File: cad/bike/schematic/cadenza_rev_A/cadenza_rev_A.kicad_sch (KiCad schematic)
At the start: 36 parts, among them J1 USB_A, J2 USB_C_Receptacle, J3 Conn_01x02, Q1 BC547, U1 TLC5916, U10 HDSP-A151, U11 TLC5916, U12 HDSP-A151, U13 STM32F105RCTx, U14 INA193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

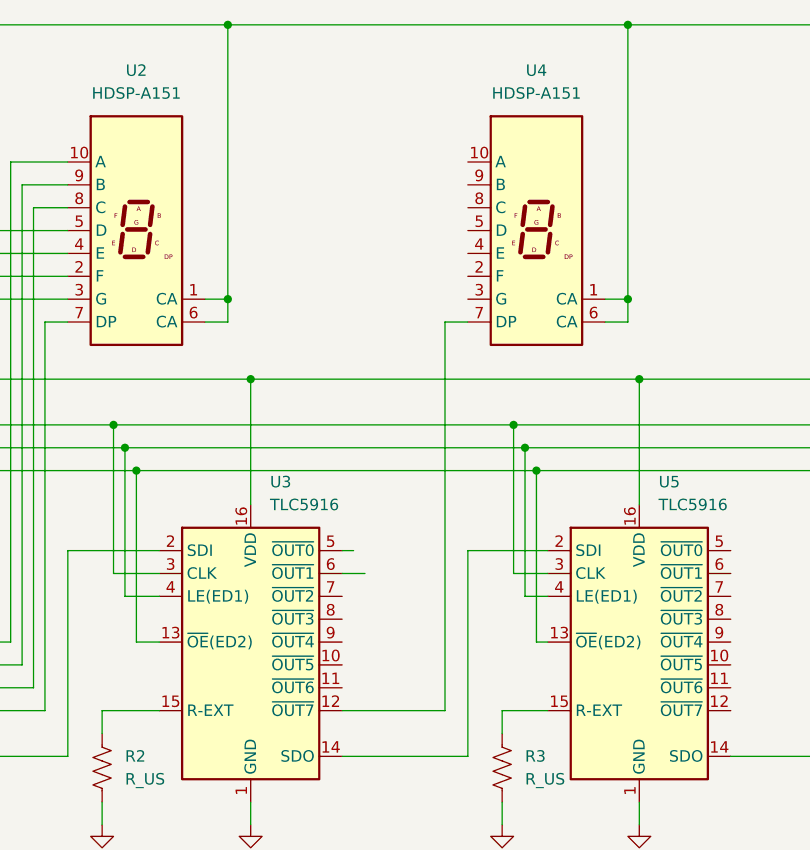
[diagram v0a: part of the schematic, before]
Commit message: rearranged parts placement
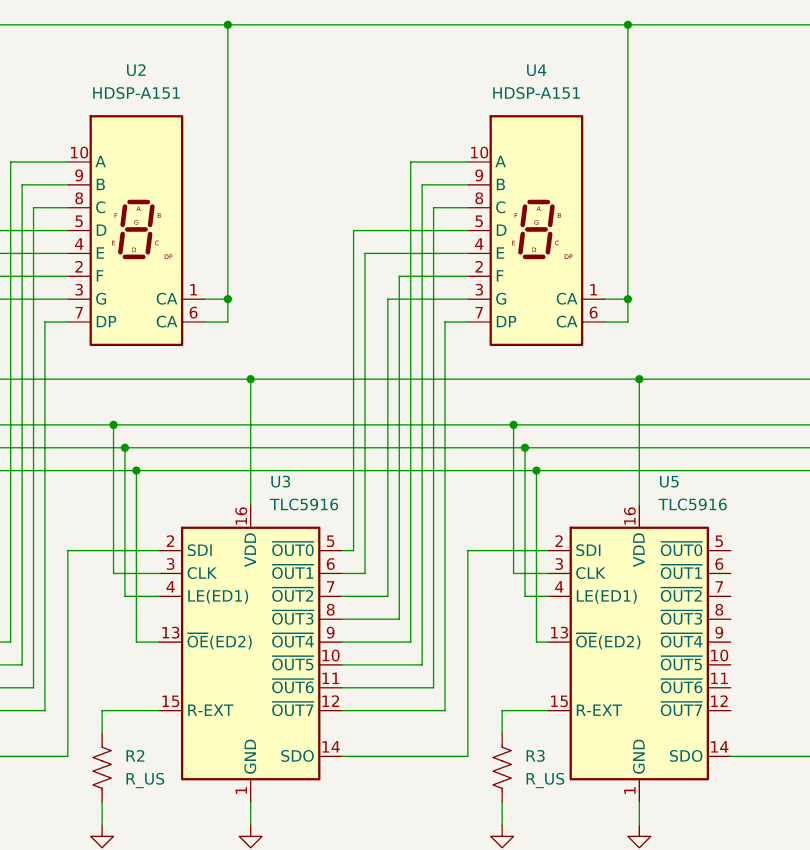
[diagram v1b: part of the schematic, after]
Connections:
- net at U4.10 (A): now also U3.9 (~{OUT4})
- net at U4.2 (F): now also U3.8 (~{OUT3})
- net at U4.3 (G): now also U3.7 (~{OUT2})
- net at U4.4 (E): now also U3.6 (~{OUT1})
- net at U4.5 (D): now also U3.5 (~{OUT0})
- net at U4.8 (C): now also U3.11 (~{OUT6})
- net at U4.9 (B): now also U3.10 (~{OUT5})
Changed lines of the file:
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@@
+	(wire
+		(pts
+			(xy 110.49 102.87) (xy 119.38 102.87)
+		)
+		(stroke
+			(width 0)
+			(type default)
+		)
+	)
 	(wire
 		(pts
@@
 	(wire
 		(pts
+			(xy 115.57 95.25) (xy 115.57 62.23)
+		)
+		(stroke
+			(width 0)
+			(type default)
+		)
+	)
+	(wire
+		(pts
 			(xy 349.25 190.5) (xy 346.71 190.5)
 		)
@@
 	(wire
 		(pts
+			(xy 113.03 57.15) (xy 124.46 57.15)
+		)
+		(stroke
+			(width 0)
+			(type default)
+		)
+	)
+	(wire
+		(pts
 			(xy 341.63 31.75) (xy 332.74 31.75)
 		)
@@
 	(wire
 		(pts
+			(xy 110.49 95.25) (xy 115.57 95.25)
+		)
+		(stroke
+			(width 0)
+			(type default)
+		)
+	)
+	(wire
+		(pts
 			(xy 41.91 118.11) (xy 41.91 120.65)
 		)
@@
 	(wire
 		(pts
+			(xy 118.11 46.99) (xy 124.46 46.99)
+		)
+		(stroke
+			(width 0)
+			(type default)
+		)
+	)
+	(wire
+		(pts
 			(xy 182.88 64.77) (xy 185.42 64.77)
 		)
@@
 	(wire
 		(pts
+			(xy 110.49 97.79) (xy 116.84 97.79)
+		)
+		(stroke
+			(width 0)
+			(type default)
+		)
+	)
+	(wire
+		(pts
 			(xy 335.28 92.71) (xy 331.47 92.71)
 		)
@@
 	(wire
 		(pts
+			(xy 118.11 100.33) (xy 118.11 46.99)
+		)
+		(stroke
+			(width 0)
+			(type default)
+		)
+	)
+	(wire
+		(pts
 			(xy 360.68 95.25) (xy 360.68 48.26)
 		)
@@
 	(wire
 		(pts
+			(xy 119.38 102.87) (xy 119.38 49.53)
+		)
+		(stroke
+			(width 0)
+			(type default)
+		)
+	)
+	(wire
+		(pts
 			(xy 228.6 31.75) (xy 271.78 31.75)
 		)
@@
 	(wire
 		(pts
+			(xy 116.84 97.79) (xy 116.84 59.69)
+		)
+		(stroke
+			(width 0)
+			(type default)
+		)
+	)
+	(wire
+		(pts
 			(xy 367.03 50.8) (xy 394.97 50.8)
 		)
@@
 	(wire
 		(pts
+			(xy 113.03 92.71) (xy 113.03 57.15)
+		)
+		(stroke
+			(width 0)
+			(type default)
+		)
+	)
+	(wire
+		(pts
 			(xy 350.52 48.26) (xy 350.52 41.91)
 		)
@@
 	(wire
 		(pts
+			(xy 111.76 90.17) (xy 111.76 54.61)
+		)
+		(stroke
+			(width 0)
+			(type default)
+		)
+	)
+	(wire
+		(pts
 			(xy 86.36 78.74) (xy 130.81 78.74)
 		)
@@
 	(wire
 		(pts
+			(xy 111.76 54.61) (xy 124.46 54.61)
+		)
+		(stroke
+			(width 0)
+			(type default)
+		)
+	)
+	(wire
+		(pts
 			(xy 377.19 48.26) (xy 377.19 41.91)
 		)
@@
 	(wire
 		(pts
+			(xy 119.38 49.53) (xy 124.46 49.53)
+		)
+		(stroke
+			(width 0)
+			(type default)
+		)
+	)
+	(wire
+		(pts
 			(xy 386.08 49.53) (xy 386.08 41.91)
 		)
@@
 	(wire
 		(pts
+			(xy 120.65 105.41) (xy 120.65 52.07)
+		)
+		(stroke
+			(width 0)
+			(type default)
+		)
+	)
+	(wire
+		(pts
 			(xy 132.08 81.28) (xy 175.26 81.28)
 		)
@@
 	(wire
 		(pts
+			(xy 110.49 100.33) (xy 118.11 100.33)
+		)
+		(stroke
+			(width 0)
+			(type default)
+		)
+	)
+	(wire
+		(pts
+			(xy 116.84 59.69) (xy 124.46 59.69)
+		)
+		(stroke
+			(width 0)
+			(type default)
+		)
+	)
+	(wire
+		(pts
+			(xy 115.57 62.23) (xy 124.46 62.23)
+		)
+		(stroke
+			(width 0)
+			(type default)
+		)
+	)
+	(wire
+		(pts
 			(xy 142.24 186.69) (xy 127 186.69)
 		)
@@
 	(wire
 		(pts
+			(xy 110.49 105.41) (xy 120.65 105.41)
+		)
+		(stroke
+			(width 0)
+			(type default)
+		)
+	)
+	(wire
+		(pts
 			(xy 346.71 193.04) (xy 349.25 193.04)
 		)
@@
 		)
 		(stroke
+			(width 0)
+			(type default)
+		)
+	)
+	(wire
+		(pts
+			(xy 120.65 52.07) (xy 124.46 52.07)
+		)
+		(stroke
